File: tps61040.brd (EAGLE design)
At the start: 12 x 17.3 mm, 10 parts, among them U1 TPS61040DBVR

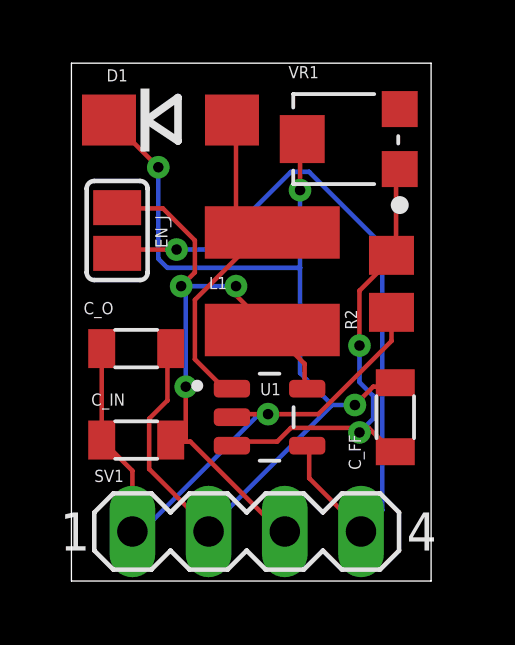
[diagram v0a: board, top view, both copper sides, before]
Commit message: switch to 0603 sized components
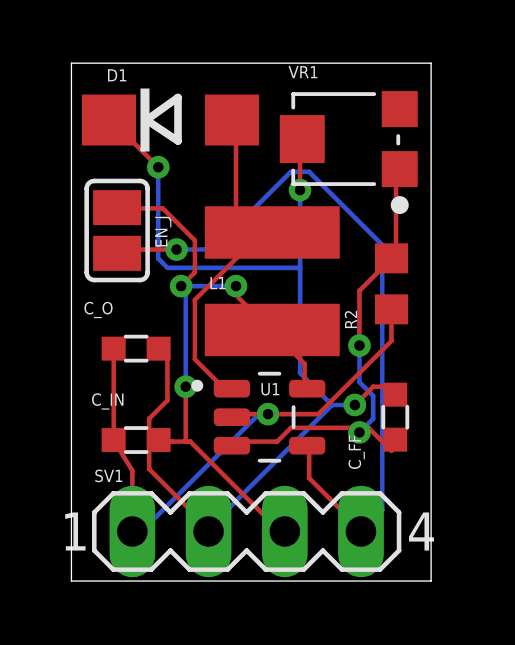
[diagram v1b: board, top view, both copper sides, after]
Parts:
- C_FF, C_IN, C_O: device Passive_Capacitors_rev15a:WCAP-CSGP_0805_WAVE -> Passive_Capacitors_rev15a:WCAP-CSGP_0603_REFLOW
- R2: device rcl:R0805 -> rcl:R0603
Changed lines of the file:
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@@
 <wire x1="11.989" y1="17.262" x2="0" y2="17.262" width="0" layer="20"/>
 <wire x1="0" y1="17.262" x2="0" y2="0" width="0" layer="20"/>
+<dimension x1="0" y1="17.262" x2="0" y2="0" x3="-1.27" y3="8.631" textsize="1.778" layer="1"/>
+<dimension x1="11.989" y1="17.262" x2="0" y2="17.262" x3="5.9945" y3="18.415" textsize="1.778" layer="1"/>
 </plain>
 <attributes>
@@
 </autorouter>
 <elements>
-<element name="C_IN" library="Passive_Capacitors_rev15a" package="WCAP-CSGP_0805_WAVE" value="4.7uF" x="2.159" y="4.699" smashed="yes">
+<element name="C_IN" library="Passive_Capacitors_rev15a" package="WCAP-CSGP_0603_REFLOW" value="4.7uF" x="2.159" y="4.699" smashed="yes">
 <attribute name="NAME" x="0.659" y="5.845" size="0.4064" layer="25"/>
 <attribute name="VALUE" x="2.564" y="5.82" size="0.4064" layer="27"/>
 </element>
-<element name="C_FF" library="Passive_Capacitors_rev15a" package="WCAP-CSGP_0805_WAVE" value="22pF" x="10.795" y="5.461" smashed="yes" rot="R90">
+<element name="C_FF" library="Passive_Capacitors_rev15a" package="WCAP-CSGP_0603_REFLOW" value="22pF" x="10.795" y="5.461" smashed="yes" rot="R90">
 <attribute name="NAME" x="9.649" y="3.707" size="0.4064" layer="25" rot="R90"/>
 <attribute name="VALUE" x="9.674" y="5.993" size="0.4064" layer="27" rot="R90"/>
 </element>
-<element name="C_O" library="Passive_Capacitors_rev15a" package="WCAP-CSGP_0805_WAVE" value="1uF" x="2.159" y="7.747" smashed="yes">
+<element name="C_O" library="Passive_Capacitors_rev15a" package="WCAP-CSGP_0603_REFLOW" value="1uF" x="2.159" y="7.747" smashed="yes">
 <attribute name="NAME" x="0.405" y="8.893" size="0.4064" layer="25"/>
 <attribute name="VALUE" x="2.945" y="8.868" size="0.4064" layer="27"/>
@@
 <attribute name="VALUE" x="10.5413" y="16.76381875" size="0.4064" layer="27"/>
 </element>
-<element name="R2" library="rcl" library_urn="urn:adsk.eagle:library:334" package="R0805" package3d_urn="urn:adsk.eagle:package:23553/2" value="1k" x="10.668" y="9.906" smashed="yes" rot="R90">
+<element name="R2" library="rcl" library_urn="urn:adsk.eagle:library:334" package="R0603" package3d_urn="urn:adsk.eagle:package:23555/3" value="1k" x="10.668" y="9.906" smashed="yes" rot="R90">
 <attribute name="NAME" x="9.525" y="8.382" size="0.4064" layer="25" rot="R90"/>
-<attribute name="POPULARITY" value="86" x="10.668" y="9.906" size="1.778" layer="27" rot="R90" display="off"/>
+<attribute name="POPULARITY" value="70" x="10.668" y="9.906" size="1.778" layer="27" rot="R90" display="off"/>
 <attribute name="SPICEPREFIX" value="R" x="10.668" y="9.906" size="1.778" layer="27" rot="R90" display="off"/>
 <attribute name="VALUE" x="9.525" y="10.541" size="0.4064" layer="27" rot="R90"/>
@@
 <wire x1="6.5532" y1="5.5626" x2="5.4864" y2="5.5626" width="0.1524" layer="1"/>
 <wire x1="10.668" y1="8.001" x2="8.2296" y2="5.5626" width="0.1524" layer="1"/>
-<wire x1="10.668" y1="8.956" x2="10.668" y2="8.001" width="0.1524" layer="1"/>
+<wire x1="10.668" y1="9.056" x2="10.668" y2="8.001" width="0.1524" layer="1"/>
 <wire x1="5.4864" y1="5.5626" x2="5.349" y2="5.461" width="0.1524" layer="1"/>
 <wire x1="2.4384" y1="1.7526" x2="2.1336" y2="1.7526" width="0.1524" layer="16"/>
@@
 <wire x1="2.1336" y1="1.7526" x2="2.032" y2="1.651" width="0.1524" layer="16"/>
 <via x="6.5532" y="5.5626" extent="1-16" drill="0.35"/>
-<wire x1="1.009" y1="7.747" x2="1.009" y2="4.699" width="0.1524" layer="1"/>
-<wire x1="1.009" y1="4.699" x2="2.032" y2="3.676" width="0.1524" layer="1"/>
+<wire x1="1.409" y1="7.747" x2="1.409" y2="4.699" width="0.1524" layer="1"/>
+<wire x1="1.409" y1="4.699" x2="2.032" y2="3.676" width="0.1524" layer="1"/>
 <wire x1="2.032" y1="3.676" x2="2.032" y2="1.651" width="0.1524" layer="1"/>
 </signal>
@@
 <wire x1="2.5908" y1="3.7338" x2="2.5908" y2="5.4102" width="0.1524" layer="1"/>
 <wire x1="4.572" y1="1.7526" x2="2.5908" y2="3.7338" width="0.1524" layer="1"/>
-<wire x1="3.2004" y1="7.6962" x2="3.309" y2="7.747" width="0.1524" layer="1"/>
+<wire x1="3.2004" y1="7.6962" x2="2.909" y2="7.747" width="0.1524" layer="1"/>
 <wire x1="4.572" y1="1.7526" x2="4.572" y2="1.651" width="0.1524" layer="1"/>
 <wire x1="10.0584" y1="6.477" x2="10.668" y2="6.477" width="0.1524" layer="1"/>
@@
 <wire x1="8.6868" y1="5.8674" x2="9.4488" y2="5.8674" width="0.1524" layer="16"/>
 <wire x1="4.572" y1="1.7526" x2="8.6868" y2="5.8674" width="0.1524" layer="16"/>
-<wire x1="10.668" y1="6.477" x2="10.795" y2="6.611" width="0.1524" layer="1"/>
+<wire x1="10.668" y1="6.477" x2="10.795" y2="6.211" width="0.1524" layer="1"/>
 <wire x1="4.572" y1="1.7526" x2="4.572" y2="1.651" width="0.1524" layer="16"/>
 <wire x1="7.62" y1="13.0302" x2="7.62" y2="14.7066" width="0.1524" layer="1"/>
@@
 <wire x1="3.81" y1="4.6482" x2="3.3528" y2="4.6482" width="0.1524" layer="1"/>
 <wire x1="7.0104" y1="1.6002" x2="3.9624" y2="4.6482" width="0.1524" layer="1"/>
-<wire x1="3.3528" y1="4.6482" x2="3.309" y2="4.699" width="0.1524" layer="1"/>
+<wire x1="3.3528" y1="4.6482" x2="2.909" y2="4.699" width="0.1524" layer="1"/>
 <wire x1="7.0104" y1="1.6002" x2="7.112" y2="1.651" width="0.1524" layer="1"/>
 <wire x1="7.7724" y1="7.239" x2="7.7724" y2="6.477" width="0.1524" layer="1"/>
@@
 <wire x1="10.668" y1="10.8966" x2="10.8204" y2="11.049" width="0.1524" layer="1"/>
 <wire x1="10.8204" y1="13.6398" x2="10.944" y2="13.732" width="0.1524" layer="1"/>
-<wire x1="10.668" y1="10.8966" x2="10.668" y2="10.856" width="0.1524" layer="1"/>
+<wire x1="10.668" y1="10.8966" x2="10.668" y2="10.756" width="0.1524" layer="1"/>
 <wire x1="6.858" y1="4.6482" x2="5.4864" y2="4.6482" width="0.1524" layer="1"/>
 <wire x1="7.3152" y1="5.1054" x2="6.858" y2="4.6482" width="0.1524" layer="1"/>
@@
 <wire x1="10.668" y1="4.3434" x2="9.906" y2="5.1054" width="0.1524" layer="1"/>
 <wire x1="5.4864" y1="4.6482" x2="5.349" y2="4.511" width="0.1524" layer="1"/>
-<wire x1="10.668" y1="4.3434" x2="10.795" y2="4.311" width="0.1524" layer="1"/>
+<wire x1="10.668" y1="4.3434" x2="10.795" y2="4.711" width="0.1524" layer="1"/>
 <wire x1="9.6012" y1="9.6774" x2="10.668" y2="10.7442" width="0.1524" layer="1"/>
 <wire x1="9.6012" y1="7.8486" x2="9.6012" y2="9.6774" width="0.1524" layer="1"/>
@@
 <wire x1="9.6012" y1="4.953" x2="10.0584" y2="5.4102" width="0.1524" layer="16"/>
 <wire x1="9.6012" y1="5.1054" x2="9.6012" y2="4.953" width="0.1524" layer="1"/>
-<wire x1="10.668" y1="10.7442" x2="10.668" y2="10.856" width="0.1524" layer="1"/>
+<wire x1="10.668" y1="10.7442" x2="10.668" y2="10.756" width="0.1524" layer="1"/>
 <via x="9.6012" y="7.8486" extent="1-16" drill="0.35"/>
 <via x="9.6012" y="4.953" extent="1-16" drill="0.35"/>

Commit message: update board to v1.1
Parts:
- removed SV1: (no value), con-lstb:MA04-1
- added EN, GND, VIN, VOUT: TPB1,27, testpad:B1,27
- added R1: Xk, rcl:R0603
- moved D1 7.36 mm to (1.40, 8.26), turned to 270 degrees
- moved R2 4.71 mm to (8.51, 5.71)
- moved VR1 3.78 mm to (6.60, 11.9)
- moved C_O 3.74 mm to (1.52, 4.06)
- moved C_FF 3.42 mm to (8.51, 2.92)
- moved L1 2.79 mm to (3.05, 5.08)
- moved C_IN 2.62 mm to (1.52, 2.16)
- moved U1 2.57 mm to (5.21, 3.30)
- moved EN_J 1.05 mm to (1.78, 12.7), turned to 180 degrees
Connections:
- net EN: now also EN.TP; no longer SV1.4
- net GND: now also GND.TP; no longer SV1.1
- net N$2: now also R1.1
- net VIN: now also VIN.TP; no longer SV1.3
- net VOUT: now also R1.2, VOUT.TP; no longer SV1.2
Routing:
- net N$1: track 11.9 -> 8.47 mm
- net VIN: track 21.7 -> 18.5 mm, vias 3 -> 2
- net VOUT: track 35.4 -> 32.3 mm, vias 3 -> 6
- net EN: track 24.5 -> 21.6 mm, vias 1 -> 2
- net N$2: track 16.1 -> 15.6 mm
- net GND: track 19.8 -> 20.2 mm, vias 1 -> 3
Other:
- board size 12 x 17.3 mm -> 9.4 x 13.7 mm
- board text added: "TPS61040 v1.1 By DoganM95"

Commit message: update to v1.2
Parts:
- removed EN, GND, VIN, VOUT: TPB1,27, testpad:B1,27
- added J2: (no value), SparkFun-Connectors:1X04_NO_SILK
- D1: value SS54 -> SS14
- R1: value Xk -> xxxk
- R2: value 1k -> 100k
- U1: value TPS61040DBVR -> TPS61040
- VR1: value 10k -> 1M
- moved EN_J 0.52 mm to (1.91, 13.2)
- moved R1 0.52 mm to (8.64, 9.27)
- moved C_IN 0.52 mm to (1.65, 2.67)
- moved C_O 0.52 mm to (1.65, 4.57)
- moved L1 0.52 mm to (3.17, 5.59)
- moved U1 0.52 mm to (5.33, 3.81)
- moved C_FF 0.52 mm to (8.64, 3.43)
- moved R2 0.52 mm to (8.64, 6.22)
- moved D1 0.52 mm to (1.52, 8.76)
- moved VR1 0.52 mm to (6.73, 12.4)
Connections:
- net EN: now also J2.4; no longer EN.TP
- net GND: now also J2.1; no longer GND.TP
- net VIN: now also J2.3; no longer VIN.TP
- net VOUT: now also J2.2; no longer VOUT.TP
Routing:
- net VOUT: track 32.3 -> 33.3 mm
- net VIN: track 18.5 -> 17.8 mm
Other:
- board size 9.4 x 13.7 mm -> 9.6 x 14.2 mm
- board text added: "EN"
- board text added: "GND"
- board text added: "TPS61040 v1.2 By DoganM95"
- board text added: "VIN"
- board text added: "VOUT"
- board text removed: "TPS61040 v1.1 By DoganM95"
